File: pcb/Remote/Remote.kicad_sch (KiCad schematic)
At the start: 7 parts, among them U1 ESP32_DevKit_V1_DOIT

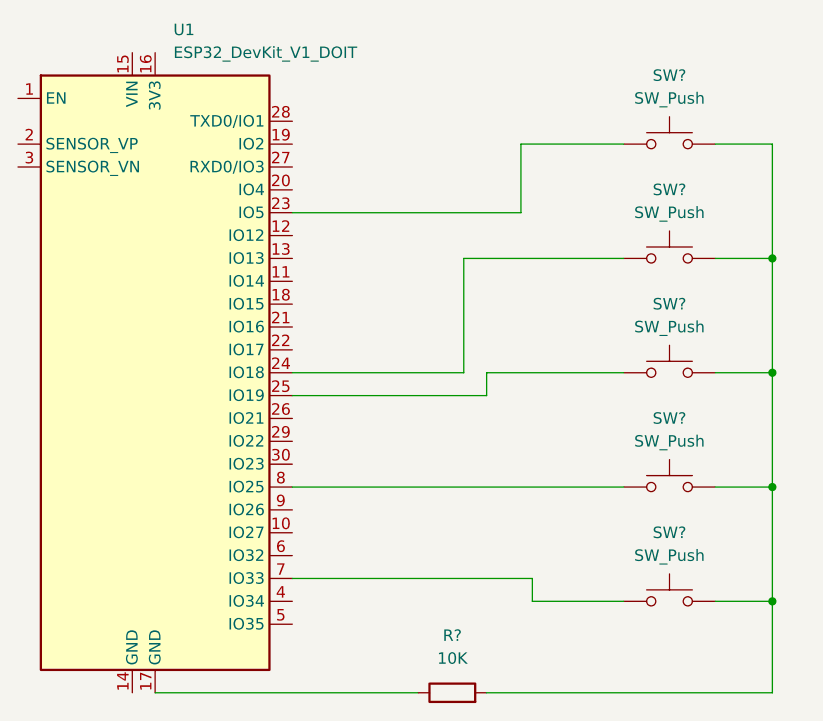
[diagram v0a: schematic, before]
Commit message: Update Remote.kicad_sch
Added a couple description to better code later down the line
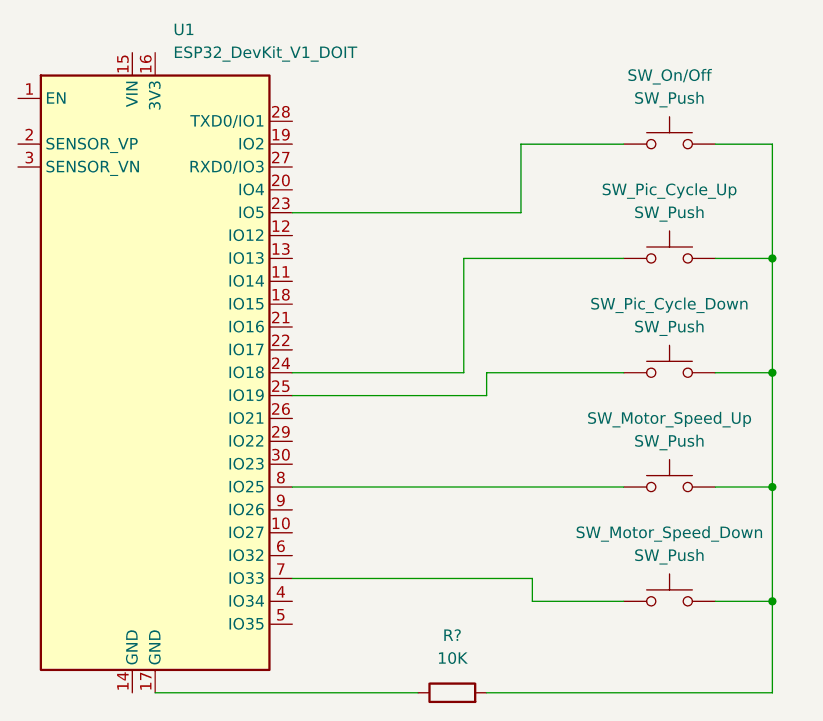
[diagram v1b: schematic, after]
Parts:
- gave numbers to parts that had none: 5
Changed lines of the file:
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@@
   (symbol (lib_id "Switch:SW_Push") (at 177.8 76.2 0) (unit 1)
     (in_bom yes) (on_board yes) (fields_autoplaced)
-    (property "Reference" "SW?" (id 0) (at 177.8 68.58 0))
+    (property "Reference" "SW_Pic_Cycle_Down" (id 0) (at 177.8 68.58 0))
     (property "Value" "SW_Push" (id 1) (at 177.8 71.12 0))
     (property "Footprint" "" (id 2) (at 177.8 71.12 0)
@@
   (symbol (lib_id "Switch:SW_Push") (at 177.8 63.5 0) (unit 1)
     (in_bom yes) (on_board yes) (fields_autoplaced)
-    (property "Reference" "SW?" (id 0) (at 177.8 55.88 0))
+    (property "Reference" "SW_Pic_Cycle_Up" (id 0) (at 177.8 55.88 0))
     (property "Value" "SW_Push" (id 1) (at 177.8 58.42 0))
     (property "Footprint" "" (id 2) (at 177.8 58.42 0)
@@
   (symbol (lib_id "Switch:SW_Push") (at 177.8 88.9 0) (unit 1)
     (in_bom yes) (on_board yes) (fields_autoplaced)
-    (property "Reference" "SW?" (id 0) (at 177.8 81.28 0))
+    (property "Reference" "SW_Motor_Speed_Up" (id 0) (at 177.8 81.28 0))
     (property "Value" "SW_Push" (id 1) (at 177.8 83.82 0))
     (property "Footprint" "" (id 2) (at 177.8 83.82 0)
@@
   (symbol (lib_id "Switch:SW_Push") (at 177.8 101.6 0) (unit 1)
     (in_bom yes) (on_board yes) (fields_autoplaced)
-    (property "Reference" "SW?" (id 0) (at 177.8 93.98 0))
+    (property "Reference" "SW_Motor_Speed_Down" (id 0) (at 177.8 93.98 0))
     (property "Value" "SW_Push" (id 1) (at 177.8 96.52 0))
     (property "Footprint" "" (id 2) (at 177.8 96.52 0)
@@
   (symbol (lib_id "Switch:SW_Push") (at 177.8 50.8 0) (unit 1)
     (in_bom yes) (on_board yes) (fields_autoplaced)
-    (property "Reference" "SW?" (id 0) (at 177.8 43.18 0))
+    (property "Reference" "SW_On/Off" (id 0) (at 177.8 43.18 0))
     (property "Value" "SW_Push" (id 1) (at 177.8 45.72 0))
     (property "Footprint" "" (id 2) (at 177.8 45.72 0)
@@
       (reference "R?") (unit 1) (value "10K") (footprint "")
     )
+    (path "/b70ad38c-77d2-48e9-b0de-833b96561dfd"
+      (reference "SW_Motor_Speed_Down") (unit 1) (value "SW_Push") (footprint "")
+    )
+    (path "/a078bdaf-7ad4-4663-aaa6-7ef9460f6c57"
+      (reference "SW_Motor_Speed_Up") (unit 1) (value "SW_Push") (footprint "")
+    )
+    (path "/c51dd1b4-0c6d-4258-ac0b-8e9e55a2f8e9"
+      (reference "SW_On/Off") (unit 1) (value "SW_Push") (footprint "")
+    )
     (path "/0e96edc7-511c-4807-b902-f127ede6d55a"
-      (reference "SW?") (unit 1) (value "SW_Push") (footprint "")
+      (reference "SW_Pic_Cycle_Down") (unit 1) (value "SW_Push") (footprint "")
     )
     (path "/8aadb536-0912-41b6-8947-16dafe2b9123"
-      (reference "SW?") (unit 1) (value "SW_Push") (footprint "")
-    )
-    (path "/a078bdaf-7ad4-4663-aaa6-7ef9460f6c57"
-      (reference "SW?") (unit 1) (value "SW_Push") (footprint "")
-    )
-    (path "/b70ad38c-77d2-48e9-b0de-833b96561dfd"
-      (reference "SW?") (unit 1) (value "SW_Push") (footprint "")
-    )
-    (path "/c51dd1b4-0c6d-4258-ac0b-8e9e55a2f8e9"
-      (reference "SW?") (unit 1) (value "SW_Push") (footprint "")
+      (reference "SW_Pic_Cycle_Up") (unit 1) (value "SW_Push") (footprint "")
     )
     (path "/6d2f6a49-b047-4653-9b58-2da1bd102bb0"

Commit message: Update Remote.kicad_sch
Updated the Pins in the schematics
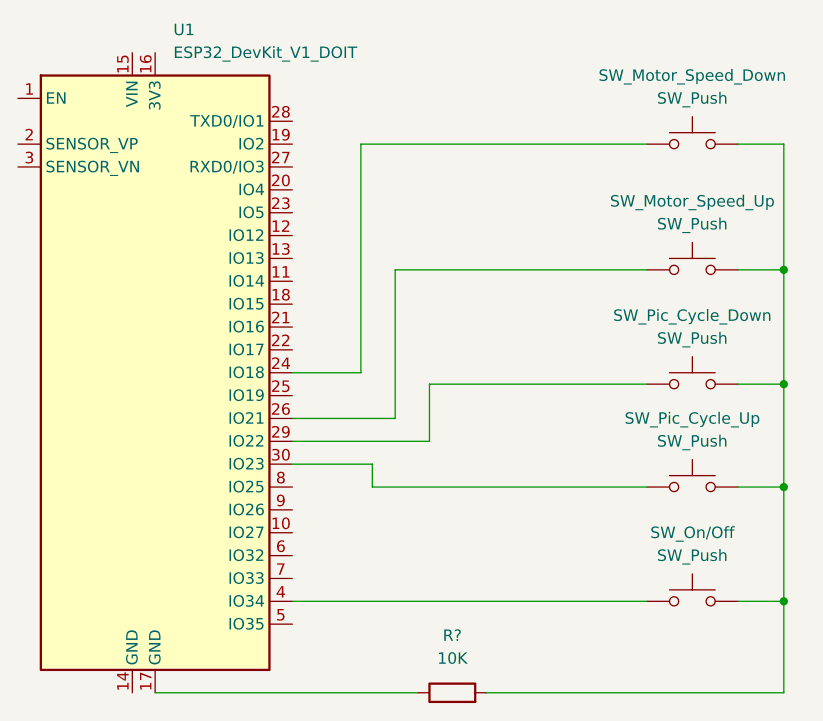
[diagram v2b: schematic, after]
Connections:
- net at SW_Pic_Cycle_Down.1: now also U1.29 (IO22); no longer U1.25 (IO19)
- net at U1.23 (IO5): no longer SW_On/Off.1
- net at U1.24 (IO18): now also SW_Motor_Speed_Down.1; no longer SW_Pic_Cycle_Up.1
- net at U1.26 (IO21): now also SW_Motor_Speed_Up.1
- net at U1.30 (IO23): now also SW_Pic_Cycle_Up.1
- net at U1.4 (IO34): now also SW_On/Off.1
- net at U1.7 (IO33): no longer SW_Motor_Speed_Down.1
- net at U1.8 (IO25): no longer SW_Motor_Speed_Up.1
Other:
- moved on the sheet: SW_Motor_Speed_Down, SW_Motor_Speed_Up, SW_On/Off, SW_Pic_Cycle_Down, SW_Pic_Cycle_Up
